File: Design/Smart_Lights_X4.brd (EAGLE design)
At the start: 80 x 80 mm, 64 parts, among them IC2 MP1584EN-LF-Z, J2 POWER_JACK, Q1 IRLR2905TRPBF, Q2 IRLR2905TRPBF, Q3 IRLR2905TRPBF, Q4 IRLR2905TRPBF, U1 ESP-32S

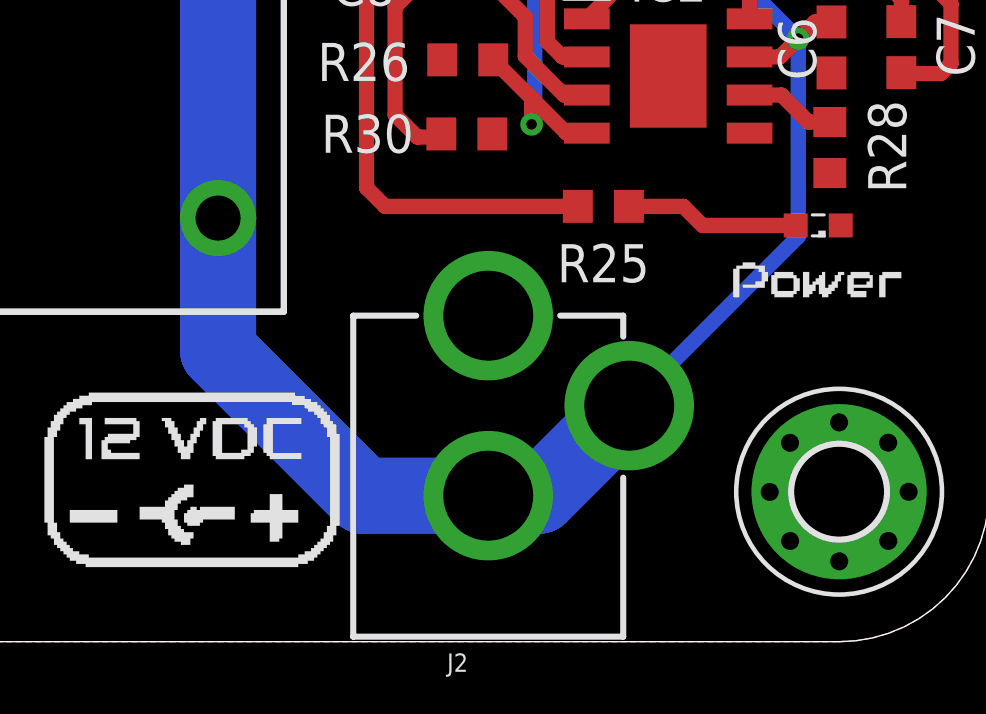
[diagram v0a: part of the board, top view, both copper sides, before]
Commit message: Fixed DC Jack connection
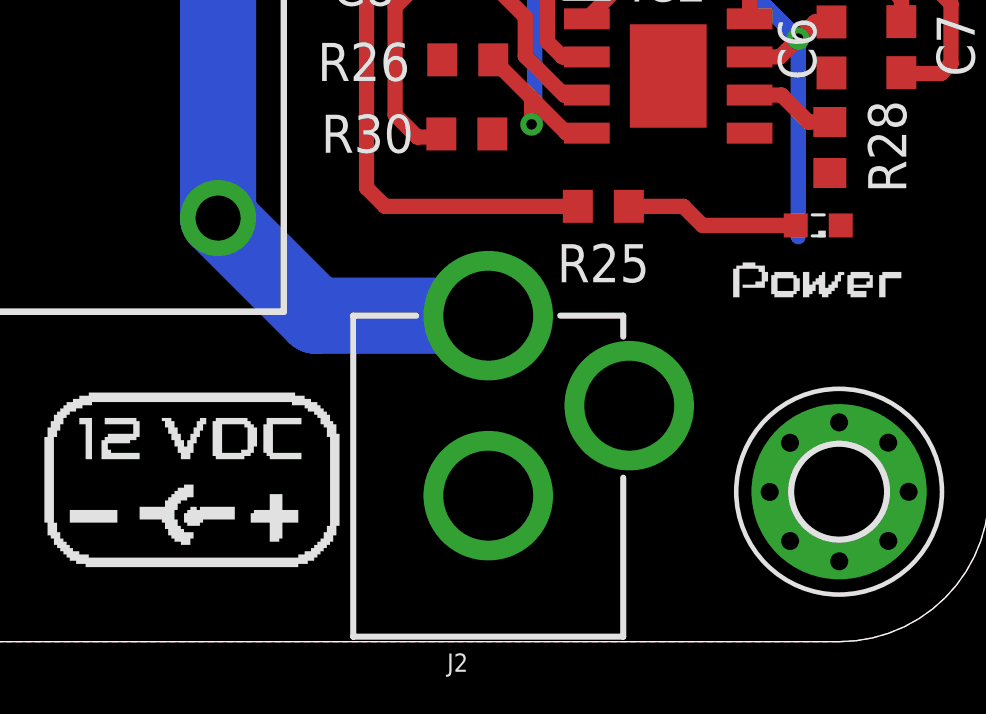
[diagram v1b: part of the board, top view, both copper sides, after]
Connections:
- net GND: now also J2.GND, J2.GNDBREAK; no longer J2.PWR
- net VCC: now also J2.PWR; no longer J2.GND, J2.GNDBREAK
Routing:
- net VCC: track 189.8 -> 170.8 mm
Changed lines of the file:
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@@
 <drawing>
 <settings>
-<setting alwaysvectorfont="yes"/>
+<setting alwaysvectorfont="no"/>
 <setting verticaltext="up"/>
 </settings>
-<grid distance="0.5" unitdist="mm" unit="mm" style="lines" multiple="1" display="yes" altdistance="5" altunitdist="mil" altunit="mil"/>
+<grid distance="0.1" unitdist="mm" unit="mm" style="lines" multiple="1" display="yes" altdistance="5" altunitdist="mil" altunit="mil"/>
 <layers>
 <layer number="1" name="Top" color="4" fill="1" visible="yes" active="yes"/>
@@
 <layer number="17" name="Pads" color="2" fill="1" visible="yes" active="yes"/>
 <layer number="18" name="Vias" color="2" fill="1" visible="yes" active="yes"/>
-<layer number="19" name="Unrouted" color="6" fill="1" visible="yes" active="yes"/>
+<layer number="19" name="Unrouted" color="6" fill="1" visible="no" active="yes"/>
 <layer number="20" name="Dimension" color="24" fill="1" visible="yes" active="yes"/>
 <layer number="21" name="tPlace" color="7" fill="1" visible="yes" active="yes"/>
@@
 <layer number="37" name="tTest" color="7" fill="1" visible="no" active="yes"/>
 <layer number="38" name="bTest" color="7" fill="1" visible="no" active="yes"/>
-<layer number="39" name="tKeepout" color="4" fill="11" visible="yes" active="yes"/>
-<layer number="40" name="bKeepout" color="1" fill="11" visible="yes" active="yes"/>
-<layer number="41" name="tRestrict" color="4" fill="10" visible="yes" active="yes"/>
-<layer number="42" name="bRestrict" color="1" fill="10" visible="yes" active="yes"/>
+<layer number="39" name="tKeepout" color="4" fill="11" visible="no" active="yes"/>
+<layer number="40" name="bKeepout" color="1" fill="11" visible="no" active="yes"/>
+<layer number="41" name="tRestrict" color="4" fill="10" visible="no" active="yes"/>
+<layer number="42" name="bRestrict" color="1" fill="10" visible="no" active="yes"/>
 <layer number="43" name="vRestrict" color="2" fill="10" visible="no" active="yes"/>
 <layer number="44" name="Drills" color="7" fill="1" visible="no" active="yes"/>
 <layer number="45" name="Holes" color="7" fill="1" visible="no" active="yes"/>
 <layer number="46" name="Milling" color="3" fill="1" visible="no" active="yes"/>
-<layer number="47" name="Measures" color="7" fill="1" visible="no" active="yes"/>
+<layer number="47" name="Measures" color="7" fill="1" visible="yes" active="yes"/>
 <layer number="48" name="Document" color="7" fill="1" visible="no" active="yes"/>
 <layer number="49" name="Reference" color="7" fill="1" visible="no" active="yes"/>
@@
 <rectangle x1="72.4201" y1="49.8847" x2="78.9797" y2="49.9905" layer="21"/>
 <rectangle x1="72.6317" y1="49.9905" x2="78.7681" y2="50.0963" layer="21"/>
+<dimension x1="5" y1="0" x2="5" y2="80" x3="-5" y3="40" textsize="2.1844" layer="47"/>
+<dimension x1="0" y1="75" x2="80" y2="75" x3="40" y3="85" textsize="2.1844" layer="47"/>
+<dimension x1="75" y1="5" x2="75" y2="0" x3="86" y3="2.5" textsize="2.1844" layer="47"/>
+<dimension x1="75" y1="5" x2="80" y2="5" x3="77.5" y3="-10" textsize="2.1844" layer="47"/>
+<dimension x1="75" y1="75" x2="79.239990625" y2="77.64999375" x3="85.854378125" y3="81.783984375" textsize="2.1844" layer="47" dtype="radius"/>
 </plain>
 <attributes>
@@
 <contactref element="C6" pad="2"/>
 <contactref element="D6" pad="A"/>
-<contactref element="J2" pad="PWR"/>
 <contactref element="PS2" pad="3"/>
 <contactref element="PS1" pad="3"/>
@@
 <via x="68.9816" y="37.7706" extent="1-16" drill="0.35"/>
 <via x="72.0498" y="40.204" extent="1-16" drill="0.35"/>
+<contactref element="J2" pad="GNDBREAK"/>
+<contactref element="J2" pad="GND"/>
 <wire x1="77.31778125" y1="74.997409375" x2="76.63784375" y2="76.63373125" width="0" layer="19" extent="1-1"/>
 <wire x1="76.6415125" y1="73.3595625" x2="75.0051875" y2="72.679625" width="0" layer="19" extent="1-1"/>
@@
 <contactref element="C6" pad="1"/>
 <contactref element="IC2" pad="7"/>
-<contactref element="J2" pad="GNDBREAK"/>
-<contactref element="J2" pad="GND"/>
 <contactref element="PS1" pad="4"/>
 <contactref element="PS2" pad="4"/>
-<wire x1="54.3" y1="14.12" x2="54.3" y2="9.7" width="2.54" layer="16"/>
-<wire x1="59.1322" y1="4.8678" x2="63.3046" y2="4.8678" width="2.54" layer="16"/>
-<wire x1="54.3" y1="9.7" x2="59.1322" y2="4.8678" width="2.54" layer="16"/>
-<wire x1="63.3046" y1="4.8678" x2="65.0046" y2="4.8678" width="2.54" layer="16"/>
-<wire x1="65.0046" y1="4.8678" x2="68.0046" y2="7.8678" width="2.54" layer="16"/>
 <wire x1="54.3" y1="14.12" x2="54.3" y2="33.5" width="2.54" layer="16"/>
 <wire x1="48.5" y1="69.5" x2="47.5" y2="70.5" width="2.54" layer="16"/>
@@
 <wire x1="72.0166" y1="19.4916" x2="73.0264" y2="19.4916" width="0.508" layer="1"/>
 <wire x1="73.0264" y1="19.4916" x2="73.6368" y2="20.102" width="0.508" layer="1"/>
-<wire x1="68.0046" y1="7.8678" x2="73.6368" y2="13.5" width="0.508" layer="16"/>
 <wire x1="73.6368" y1="13.5" x2="73.6368" y2="20.102" width="0.508" layer="16"/>
 <wire x1="66.1792" y1="25.2664" x2="67.5864" y2="25.2664" width="0.508" layer="1"/>
@@
 <wire x1="43" y1="70.5" x2="43.4036" y2="70.9036" width="2.54" layer="16"/>
 <wire x1="43.4036" y1="70.9036" x2="43.4036" y2="75.1762" width="2.54" layer="16"/>
+<contactref element="J2" pad="PWR"/>
+<wire x1="54.3" y1="14.12" x2="57.5522" y2="10.8678" width="2.54" layer="16"/>
+<wire x1="57.5522" y1="10.8678" x2="63.3046" y2="10.8678" width="2.54" layer="16"/>
+<wire x1="63.3046" y1="10.8678" x2="73.6368" y2="13.5" width="0" layer="19" extent="16-16"/>
 </signal>
 <signal name="N$1">

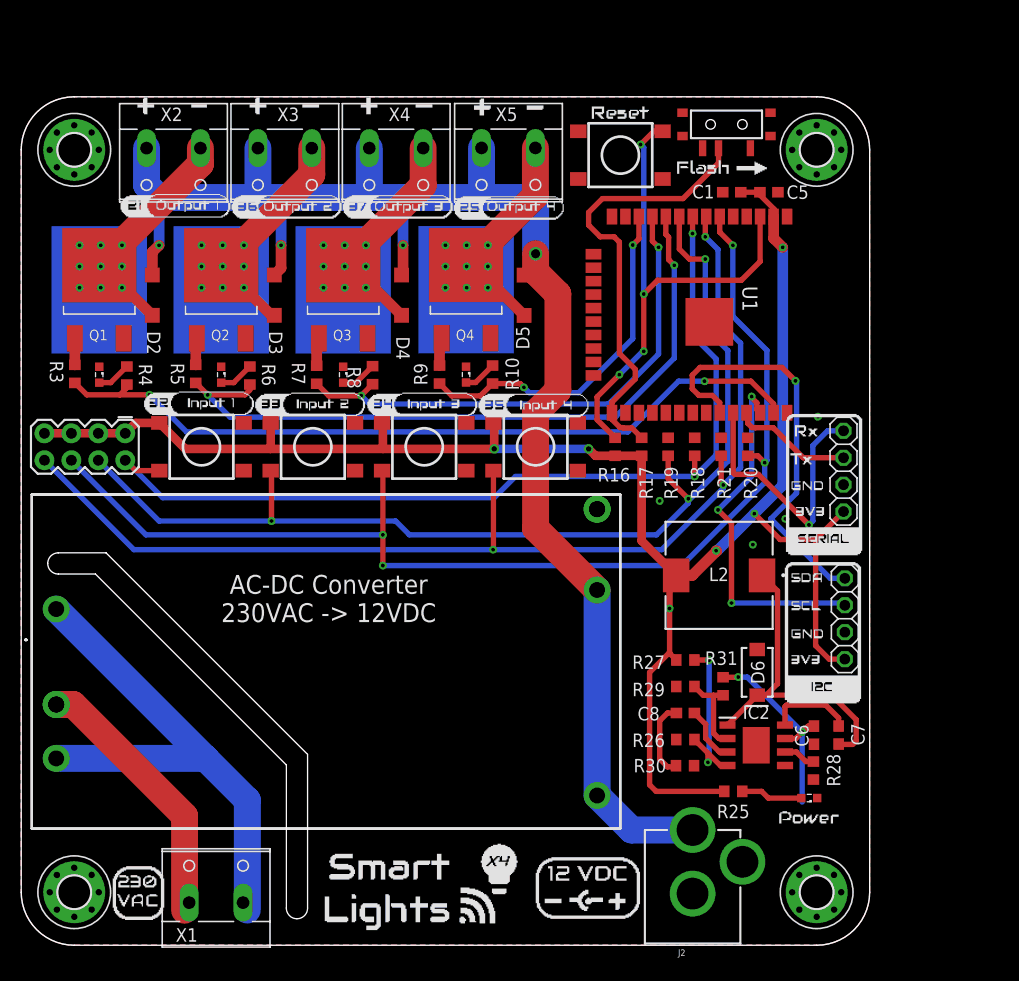
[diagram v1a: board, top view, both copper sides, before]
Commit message: Resize dimensions to fit in the 92x87 enclosure
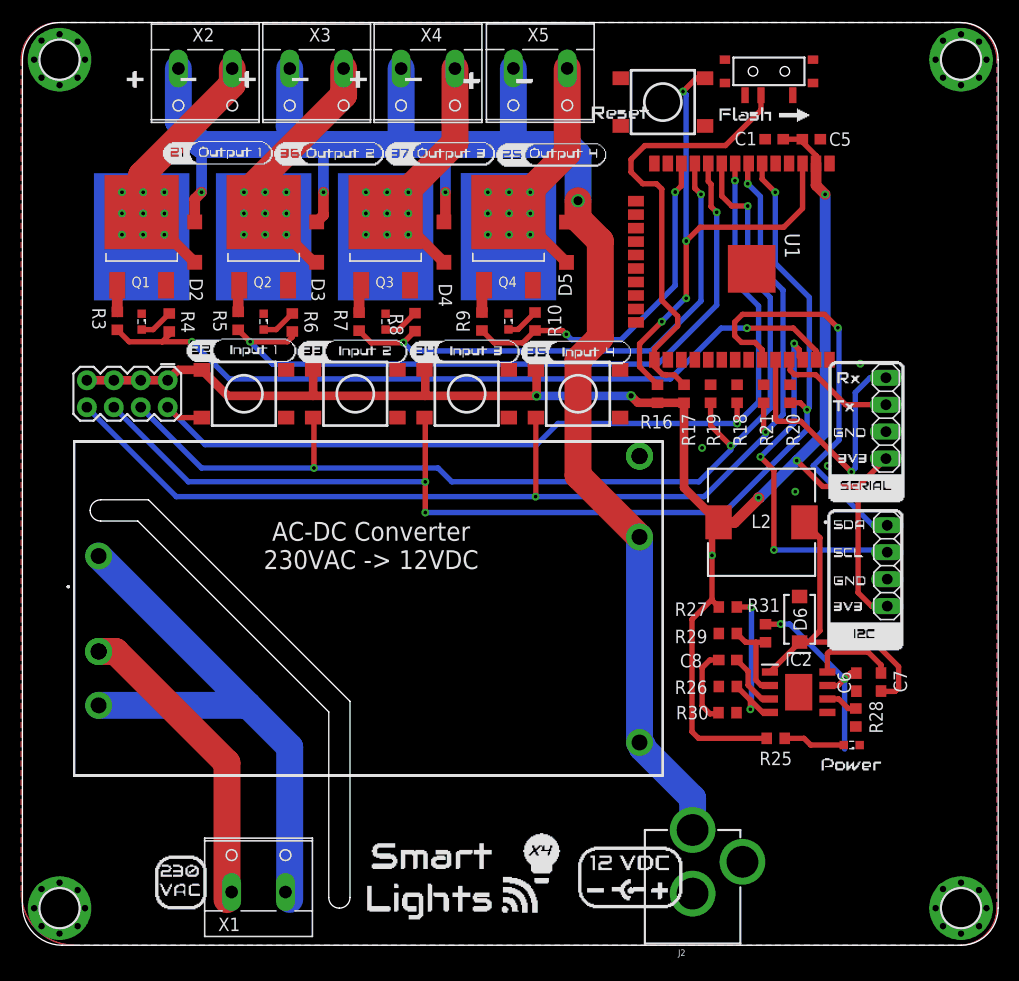
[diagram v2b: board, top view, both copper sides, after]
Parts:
- removed H1, H2, H3, H4: MOUNT-PAD-ROUND, SpaceDIY_connectors:3,0-PAD
- added FRAME1: (no value), SpaceDIY_symbols:92X87
- moved X2 8.08 mm to (17.4, 82.0)
- moved X3 8.08 mm to (27.9, 82.0)
- moved X4 8.08 mm to (38.4, 82.0)
- moved X5 8.08 mm to (48.9, 82.0)
- moved D5 6.40 mm to (51.4, 66.3)
- moved LED4 6.40 mm to (34.4, 58.8)
- moved Q3 6.40 mm to (34.4, 66.8)
- moved R25 6.40 mm to (71.1, 19.5)
- moved C1 6.40 mm to (71.0, 76.0)
- moved C5 6.40 mm to (74.5, 76.0)
- moved C6 6.40 mm to (78.7, 24.8)
- moved C7 6.40 mm to (81.1, 24.8)
- moved C8 6.40 mm to (66.6, 26.9)
- moved D2 6.40 mm to (16.4, 66.3)
- moved D3 6.40 mm to (27.9, 66.3)
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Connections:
- net GND: now also FRAME1.B3,1, FRAME1.B3,2, FRAME1.B3,3, FRAME1.B3,6; no longer H1.B3,0, H1.P$2, H1.P$3, H1.P$4, H1.P$5, H1.P$6, H1.P$7, H1.P$8, H1.P$9, H2.B3,0, H2.P$2, H2.P$3, H2.P$4, H2.P$5, H2.P$6, H2.P$7, H2.P$8, H2.P$9, H3.B3,0, H3.P$2, H3.P$3, H3.P$4, H3.P$5, H3.P$6, H3.P$7, H3.P$8, H3.P$9, H4.B3,0, H4.P$2, H4.P$3, H4.P$4, H4.P$5, H4.P$6, H4.P$7, H4.P$8, H4.P$9
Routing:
- net VCC: track 170.8 -> 182.0 mm
- net N$6: track 21.5 -> 25.6 mm
- net N$3: track 49.9 -> 53.9 mm
- net N$2: track 25.3 -> 29.3 mm
- net N$10: track 21.2 -> 23.3 mm
- net N$8: track 21.6 -> 23.7 mm
- net N$4: track 22.9 -> 24.0 mm
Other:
- board size 80 x 80 mm -> 92 x 87 mm
